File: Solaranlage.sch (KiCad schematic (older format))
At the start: 77 parts, among them J1 Screw_Terminal_01x02, J2 Screw_Terminal_01x02, J3 AVR-JTAG-10, J4 USB_B, J5 USB_B, J6 Screw_Terminal_01x02, Q1 2N3904, Q2 BC328, SW1 Rotary_Encoder_Switch_Panason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, SW2 SW_SPDT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

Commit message: resized schematic sheet
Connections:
- wire segments 374 -> 376
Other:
- moved on the sheet: C1, C10, C11, C12, C13, C14, C15, C16, C17, C18, C19, C2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

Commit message: removed Q2. Had no plan why it was added. Inserted jumper to disable watchdog during sw-development
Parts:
- removed Q2: BC328, Package_TO_SOT_THT:TO-92_HandSolder, symbol Transistor_BJT:BC328
- added JP1: Jumper, Connector_PinHeader_2.54mm:PinHeader_1x03_P2.54mm_Vertical, symbol Device:Jumper
- Q1: footprint Package_TO_SOT_THT:TO-92_HandSolder -> Package_TO_SOT_THT:TO-92L_Wide
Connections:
- wire segments 376 -> 375
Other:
- note added: "Watchdog disable\n"
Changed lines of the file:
@@
 Wire Wire Line
 	13250 12350 13250 12000
-Wire Wire Line
-	13250 12000 13850 12000
 Connection ~ 14850 12000
 Wire Wire Line
@@
 	1    0    0    -1
 $EndComp
-Wire Wire Line
-	13850 12750 13850 13000
-Wire Wire Line
-	13850 12350 13850 12000
-Connection ~ 13850 12000
-Wire Wire Line
-	13850 12000 14850 12000
-Text GLabel 14200 12550 2    50   Input ~ 0
-\RST
-Wire Wire Line
-	14200 12550 14150 12550
 $Comp
 L Transistor_BJT:2N3904 Q1
@@
 F 0 "Q1" H 13100 12750 50  0000 L CNN
 F 1 "2N3904" H 12900 12400 50  0000 L CNN
-F 2 "Package_TO_SOT_THT:TO-92_HandSolder" H 13350 12475 50  0001 L CIN
+F 2 "Package_TO_SOT_THT:TO-92L_Wide" H 13350 12475 50  0001 L CIN
 F 3 "https://www.fairchildsemi.com/datasheets/2N/2N3904.pdf" H 13150 12550 50  0001 L CNN
 	1    13150 12550
 	1    0    0    -1
-$EndComp
-$Comp
-L Transistor_BJT:BC328 Q2
-U 1 1 5FF9EB7A
-P 13950 12550
-F 0 "Q2" H 14141 12596 50  0000 L CNN
-F 1 "BC328" H 14141 12505 50  0000 L CNN
-F 2 "Package_TO_SOT_THT:TO-92_HandSolder" H 14150 12475 50  0001 L CIN
-F 3 "http://www.redrok.com/PNP_BC327_-45V_-800mA_0.625W_Hfe100_TO-92.pdf" H 13950 12550 50  0001 L CNN
-	1    13950 12550
-	-1   0    0    -1
 $EndComp
 Wire Wire Line
@@
 	5350 3450 13000 3450
 Connection ~ 4700 4700
+$Comp
+L Device:Jumper JP1
+U 1 1 6018D25C
+P 13850 12500
+F 0 "JP1" V 13804 12627 50  0000 L CNN
+F 1 "Jumper" V 13895 12627 50  0000 L CNN
+F 2 "Connector_PinHeader_2.54mm:PinHeader_1x03_P2.54mm_Vertical" H 13850 12500 50  0001 C CNN
+F 3 "~" H 13850 12500 50  0001 C CNN
+	1    13850 12500
+	0    1    1    0
+$EndComp
+Wire Wire Line
+	13250 12000 13850 12000
+Wire Wire Line
+	13850 12200 13850 12000
+Connection ~ 13850 12000
+Wire Wire Line
+	13850 12000 14850 12000
+Wire Wire Line
+	13850 12800 13850 13000
+Text Notes 13950 12300 0    50   ~ 0
+Watchdog disable\n
 $EndSCHEMATC

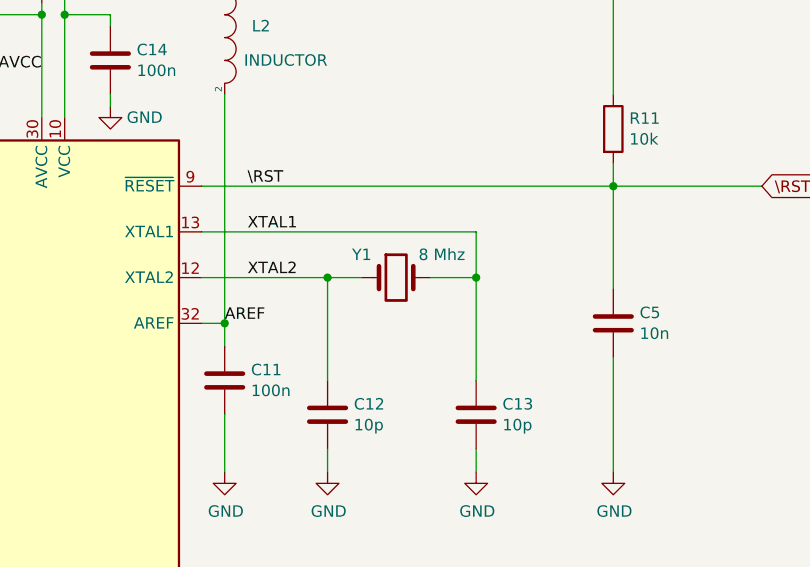
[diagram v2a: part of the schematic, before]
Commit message: fixed frequency of crystal in schematic
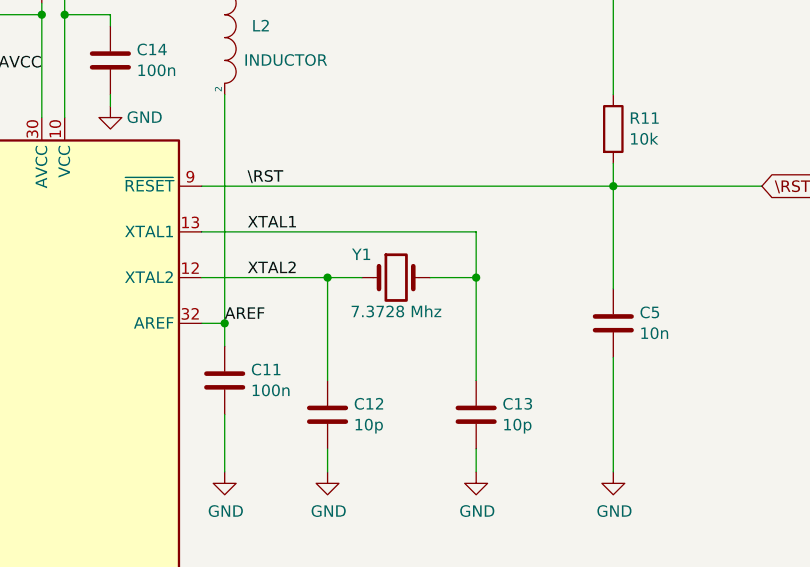
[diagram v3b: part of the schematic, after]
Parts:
- Y1: value 8 Mhz -> 7.3728 Mhz
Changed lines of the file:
@@
 P 15050 3850
 F 0 "Y1" H 14900 3950 50  0000 C CNN
-F 1 "8 Mhz" H 15250 3950 50  0000 C CNN
+F 1 "7.3728 Mhz" H 15050 3700 50  0000 C CNN
 F 2 "Crystal:Crystal_HC18-U_Vertical" H 15050 3850 50  0001 C CNN
 F 3 "~" H 15050 3850 50  0001 C CNN

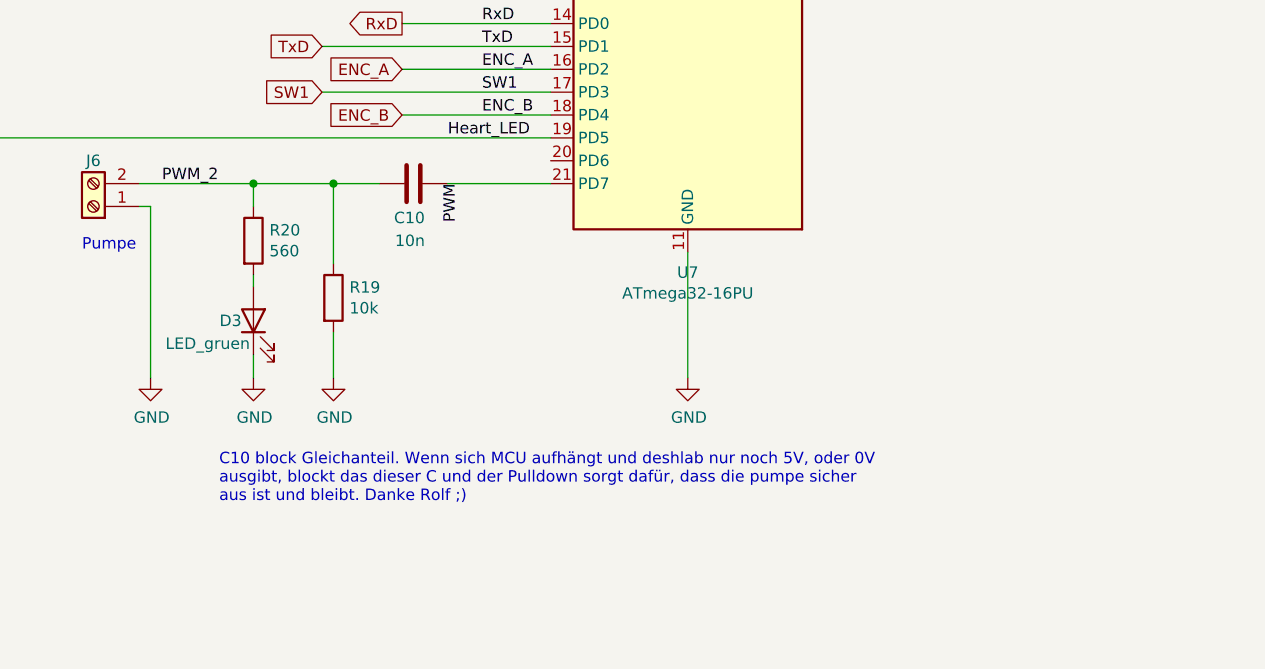
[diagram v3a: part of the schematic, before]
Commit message: removed C10 (for common mode blocking of pwm in case of stalling output), because the pwm frequency had to be lowered to 30 Hz
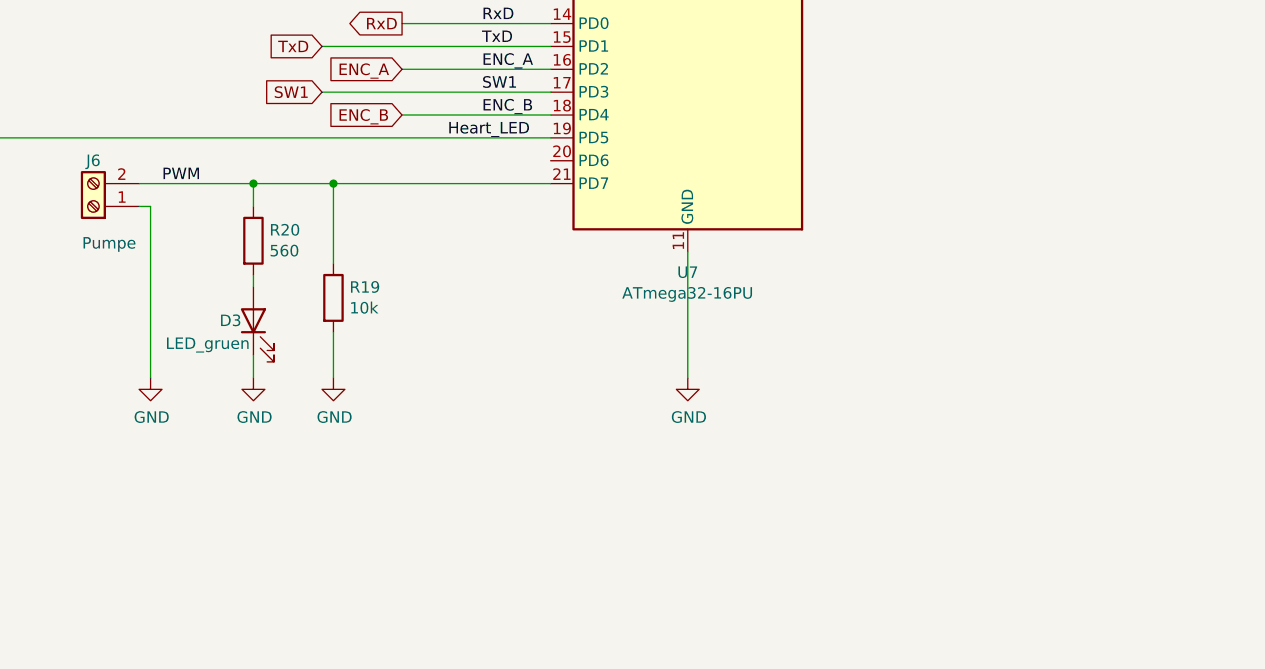
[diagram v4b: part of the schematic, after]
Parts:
- removed C10: 10n, Capacitor_THT:C_Disc_D4.7mm_W2.5mm_P5.00mm, symbol Device:C
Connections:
- net PWM_2 is gone; now on net PWM: J6.2 (Pin_2), R19.1, R20.1
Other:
- note removed: "C10 block Gleichanteil. Wenn sich MCU aufhängt und deshlab nur noch 5V, oder 0V\nausgibt, blockt das dieser C und der Pulldown sorgt dafür, dass die pumpe sicher\naus ist und bleibt. Danke Rolf ;)\n"
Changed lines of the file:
@@
 Wire Wire Line
 	11700 6850 12050 6850
-Wire Wire Line
-	12050 6850 12250 6850
 Connection ~ 12050 6850
 Wire Wire Line
@@
 $EndComp
 Text Label 11300 6850 0    50   ~ 0
-PWM_2
-Text Label 12600 6850 3    50   ~ 0
 PWM
 $Comp
@@
 	1    12050 7350
 	1    0    0    -1
-$EndComp
-Text Notes 11550 8250 0    50   ~ 0
-C10 block Gleichanteil. Wenn sich MCU aufhängt und deshlab nur noch 5V, oder 0V\nausgibt, blockt das dieser C und der Pulldown sorgt dafür, dass die pumpe sicher\naus ist und bleibt. Danke Rolf ;)\n
-$Comp
-L Device:C C10
-U 1 1 5FE38FCD
-P 12400 6850
-F 0 "C10" V 12550 6800 50  0000 L CNN
-F 1 "10n" V 12650 6800 50  0000 L CNN
-F 2 "Capacitor_THT:C_Disc_D4.7mm_W2.5mm_P5.00mm" H 12438 6700 50  0001 C CNN
-F 3 "~" H 12400 6850 50  0001 C CNN
-	1    12400 6850
-	0    -1   1    0
 $EndComp
 Text Label 12550 6650 0    50   ~ 0
@@
 $EndComp
 Wire Wire Line
-	12550 6850 13000 6850
-Wire Wire Line
 	10350 6650 10350 6900
 Wire Wire Line
@@
 Text Notes 13950 12300 0    50   ~ 0
 Watchdog disable\n
+Wire Wire Line
+	12050 6850 13000 6850
 $EndSCHEMATC

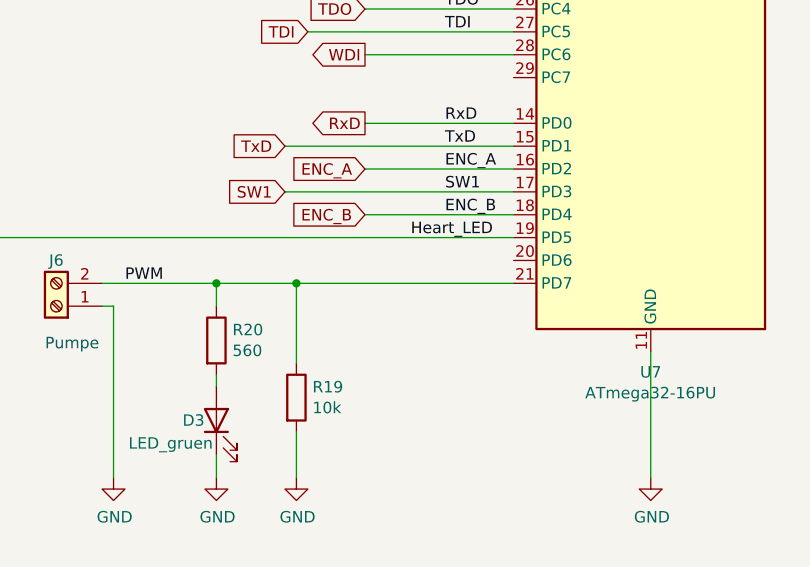
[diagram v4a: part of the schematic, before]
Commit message: added 1k serial resistance in the PWM output line to protect GPIO PD7 from burning down
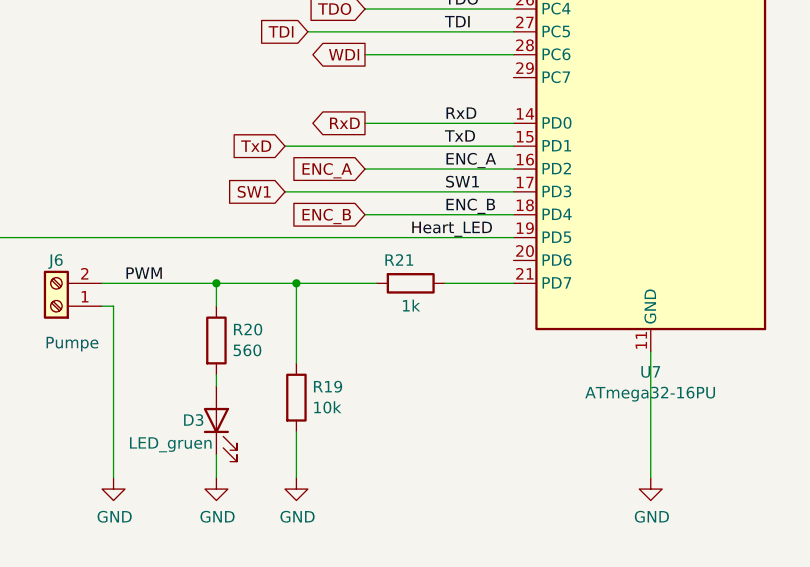
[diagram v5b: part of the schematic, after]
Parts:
- added R21: 1k, Resistor_THT:R_Axial_DIN0204_L3.6mm_D1.6mm_P7.62mm_Horizontal, symbol Device:R
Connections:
- net PWM: now also R21.2; no longer U7.21 (PD7)
- new net: R21.1, U7.21 (PD7)
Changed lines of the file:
@@
 Watchdog disable\n
 Wire Wire Line
-	12050 6850 13000 6850
+	12050 6850 12400 6850
+$Comp
+L Device:R R21
+U 1 1 60379EAF
+P 12550 6850
+F 0 "R21" V 12450 6800 50  0000 C CNN
+F 1 "1k" V 12650 6850 50  0000 C CNN
+F 2 "Resistor_THT:R_Axial_DIN0204_L3.6mm_D1.6mm_P7.62mm_Horizontal" V 12480 6850 50  0001 C CNN
+F 3 "~" H 12550 6850 50  0001 C CNN
+	1    12550 6850
+	0    1    1    0
+$EndComp
+Wire Wire Line
+	12700 6850 13000 6850
 $EndSCHEMATC

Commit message: added LEDs to indicate what the displays show at the moment; added some 3D models; added 10k serial resistors to opamp-outs for TP
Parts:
- added D4: TD, LED_THT:LED_D3.0mm, symbol Device:LED
- added D5: TK, LED_THT:LED_D3.0mm, symbol Device:LED
- added D6: d1, LED_THT:LED_D3.0mm, symbol Device:LED
- added D7: d2, LED_THT:LED_D3.0mm, symbol Device:LED
- added R25, R26, R27, R28: 330, Resistor_THT:R_Axial_DIN0204_L3.6mm_D1.6mm_P7.62mm_Horizontal, symbol Device:R
- added R29, R30: 10k, Resistor_THT:R_Axial_DIN0204_L3.6mm_D1.6mm_P7.62mm_Horizontal, symbol Device:R
- C17, C19: value 10n -> 100n
- H1, H2, H3, H4, H5, H6: symbol Mechanical:MountingHole -> Mechanical:MountingHole_Pad
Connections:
- net DACH_ADC: now also R29.1; no longer RV1.1, U9.1
- net GND: now also H1.1, H2.1, H3.1, H4.1, H5.1, H6.1, R25.2, R26.2, R27.2, R28.2
- net KELLER_ADC: now also R30.1; no longer RV2.1, U9.7
- net delta2: now reaches U7.20 (PD6)
- net delta2: now also D4.2 (A)
- net temp_dach: now reaches U7.22 (PC0)
- net temp_dach: now also D7.2 (A)
- net temp_keller: now reaches U7.23 (PC1)
- net temp_keller: now also D6.2 (A)
- net delta1: now reaches U7.29 (PC7)
- net delta1: now also D5.2 (A)
- new net: R29.2, RV1.1, U9.1
- new net: R30.2, RV2.1, U9.7
- new net: D4.1 (K), R25.1
- new net: D5.1 (K), R26.1
- new net: D6.1 (K), R27.1
- new net: D7.1 (K), R28.1

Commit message: adapted remarks from schematic review; added output buffer to PWM output
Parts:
- removed C11: 100n, Capacitor_THT:C_Disc_D4.7mm_W2.5mm_P5.00mm, symbol Device:C
- removed R12, R13: 22, Resistor_THT:R_Axial_DIN0204_L3.6mm_D1.6mm_P7.62mm_Horizontal, symbol Device:R
- removed R19: 10k, Resistor_THT:R_Axial_DIN0204_L3.6mm_D1.6mm_P7.62mm_Horizontal, symbol Device:R
- removed R21: 1k, Resistor_THT:R_Axial_DIN0204_L3.6mm_D1.6mm_P7.62mm_Horizontal, symbol Device:R
- added C10, C21: 100n, Capacitor_THT:C_Disc_D4.7mm_W2.5mm_P5.00mm, symbol Device:C
- added C11: 13uF, Capacitor_THT:CP_Radial_D6.3mm_P2.50mm, symbol Device:CP
- added C22: 100n, Capacitor_THT:C_Rect_L7.0mm_W2.0mm_P5.00mm, symbol Device:C
- added U11: 74LS125, Package_DIP:DIP-14_W7.62mm, symbol 74xx:74LS125
- C18: value 10u1 -> 13uF; footprint Capacitor_THT:CP_Radial_D8.0mm_P5.00mm -> Capacitor_THT:CP_Radial_D6.3mm_P2.50mm
- L1: value INDUCTOR -> 10uH; footprint Inductor_THT:L_Radial_D10.0mm_P5.00mm_Fastron_07P -> Inductor_THT:L_Axial_L9.5mm_D4.0mm_P5.08mm_Vertical_Fastron_SMCC
- L2: value INDUCTOR -> 10u; footprint Inductor_THT:L_Radial_D10.0mm_P5.00mm_Fastron_07P -> Inductor_THT:L_Axial_L9.5mm_D4.0mm_P5.08mm_Vertical_Fastron_SMCC
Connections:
- net +5V: now also U11.14 (VCC)
- net AREF: now also C11.1
- net DACH_ADC: now also C10.1
- net GND: now also C10.2, C11.2, C21.2, C22.2, U11.7 (GND)
- net KELLER_ADC: now also C21.1
- net PWM: now also U7.21 (PD7), U11.12, U11.2, U11.5, U11.9; no longer J6.2 (Pin_2), R20.1
- net \RST: now also U11.1, U11.10, U11.13, U11.4
- net at U8.15 (USBD+): now also J4.3 (D+)
- net at U8.16 (USBD-): now also J4.2 (D-)
- net at U8.17 (3V3OUT): now also C22.1
- new net PWM2: J6.2 (Pin_2), R20.1, U11.11, U11.3, U11.6, U11.8
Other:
- note removed: "sould be left N.C.\n"
- moved on the sheet: C12, C13, C14, C5, D2, D3, D4, D5, D6, D7, J6, L1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

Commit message: added some datasheets and ordering numbers
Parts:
- added D10, D11, D8, D9: D_TVS, Diode_THT:D_DO-201_P3.81mm_Vertical_KathodeUp, symbol Device:D_TVS
- added R12, R13, R19, R21: 1k, Resistor_THT:R_Axial_DIN0204_L3.6mm_D1.6mm_P7.62mm_Horizontal, symbol Device:R
- D4: Ordering (none) -> Conrad: 1573698 - 62
- D5: value TK -> TD; Ordering (none) -> Conrad: 1573698 - 62
- D6: value d1 -> TD; Ordering (none) -> Conrad: 1573698 - 62
- D7: value d2 -> TD; Ordering (none) -> Conrad: 1573698 - 62
- J3: Ordering (none) -> Conrad: 1303517 - 62
- L2: value 10u -> 10uH
- SW1: Ordering (none) -> Digikey: P12423-ND
- SW2: Ordering (none) -> Digikey: EG2355-ND
- U1, U2, U3, U4, U5, U6: Ordering (none) -> Reichelt: C 56-11 RT
- U11: Ordering (none) -> Reichelt: LS 125
- U7: Ordering (none) -> Conrad: 812265799 - 62
- U9: value TS912 -> MCP6002-I/P; Ordering (none) -> Conrad: 651489 - 62
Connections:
- net GND: now also D10.2 (A2), D11.2 (A2), D8.2 (A2), D9.2 (A2)
- net PWM2: now also D11.1 (A1), R12.2, R13.2, R19.2, R21.2; no longer U11.11, U11.3, U11.6, U11.8
- net at C3.1, J1.2 (Pin_2), R1.2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: now also D8.1 (A1)
- net at C4.1, J2.2 (Pin_2), R2.2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: now also D9.1 (A1)
- net at J5.1 (VBUS), SW2.2 (B): now also D10.1 (A1)
- new net: R12.1, U11.3
- new net: R13.1, U11.6
- new net: R19.1, U11.8
- new net: R21.1, U11.11
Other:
- note added: "k = 5.9"
- note added: "tau = 2 ms"
- note removed: "1.449 k"
- note removed: "8.550 k"
- note removed: "k = 6.9"
- moved on the sheet: C1, C11, C12, C13, C14, C15, C16, C18, C2, C22, C5, C7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
